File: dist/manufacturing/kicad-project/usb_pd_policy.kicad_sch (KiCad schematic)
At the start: 20 parts, among them Q2 CSD17484F4, Q3 CSD17484F4, U2 TPS26750SRSMR, U3 M24512-RMN6TP

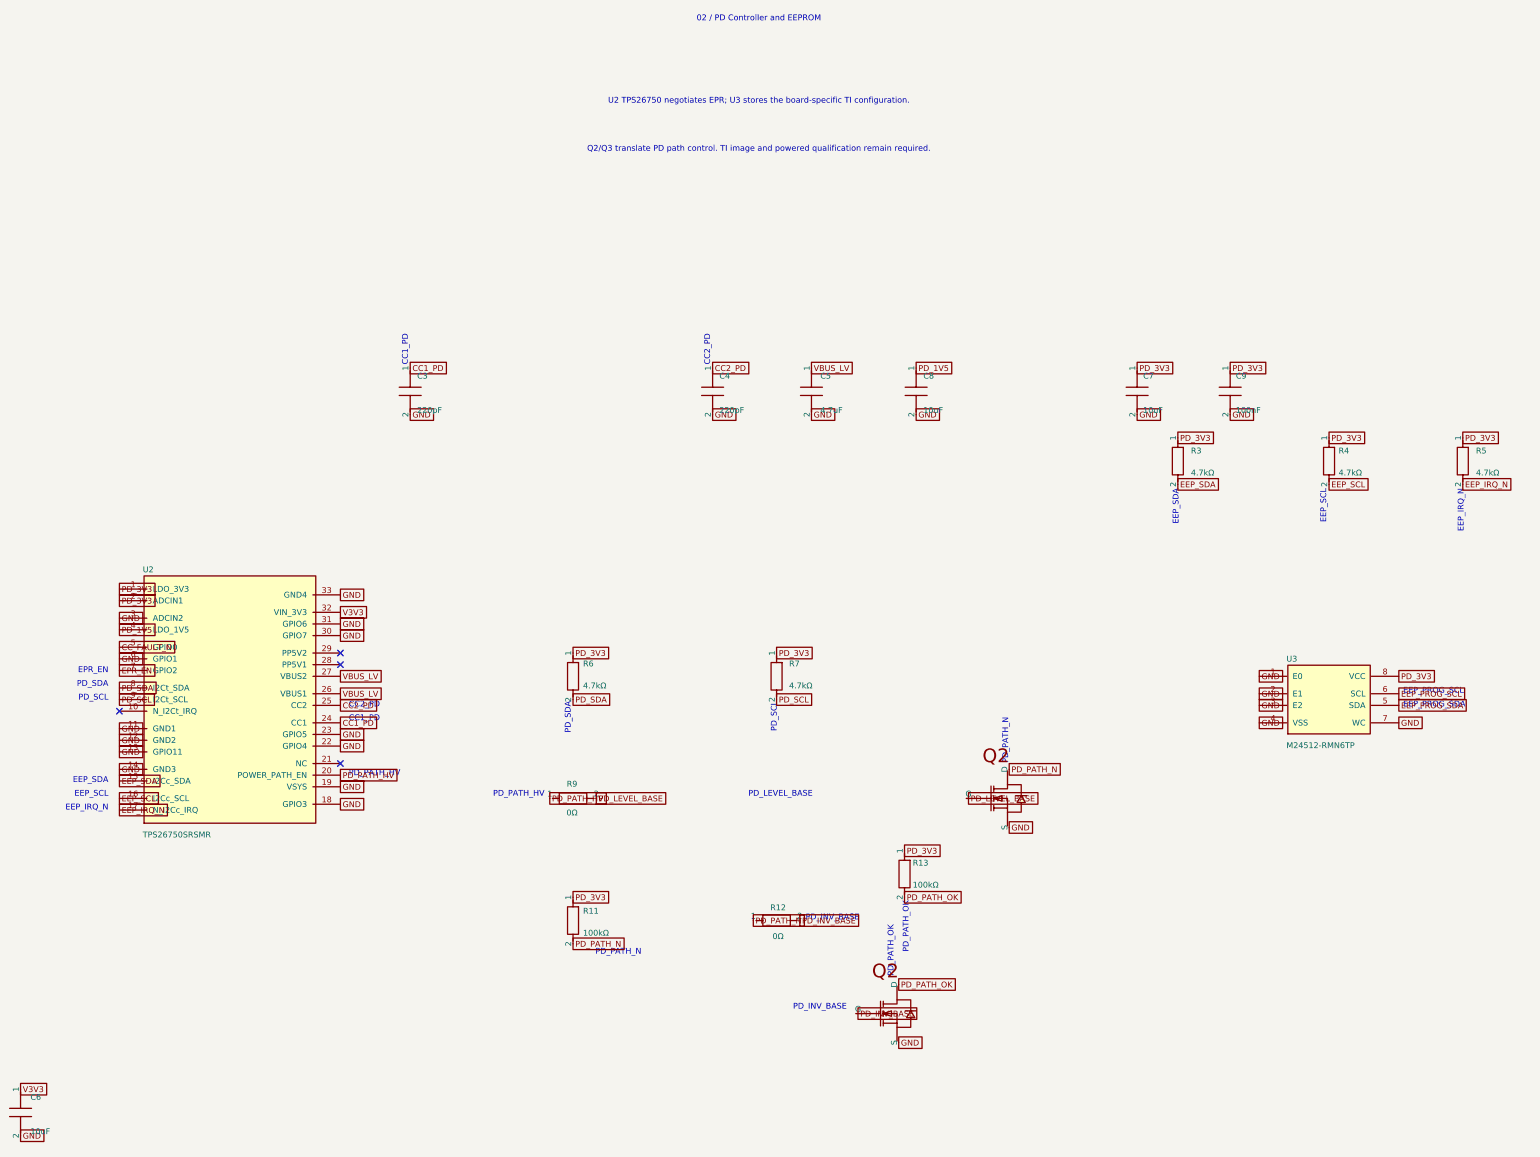
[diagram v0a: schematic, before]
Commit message: Implement motor harness and mounting; remove unsupported interfaces
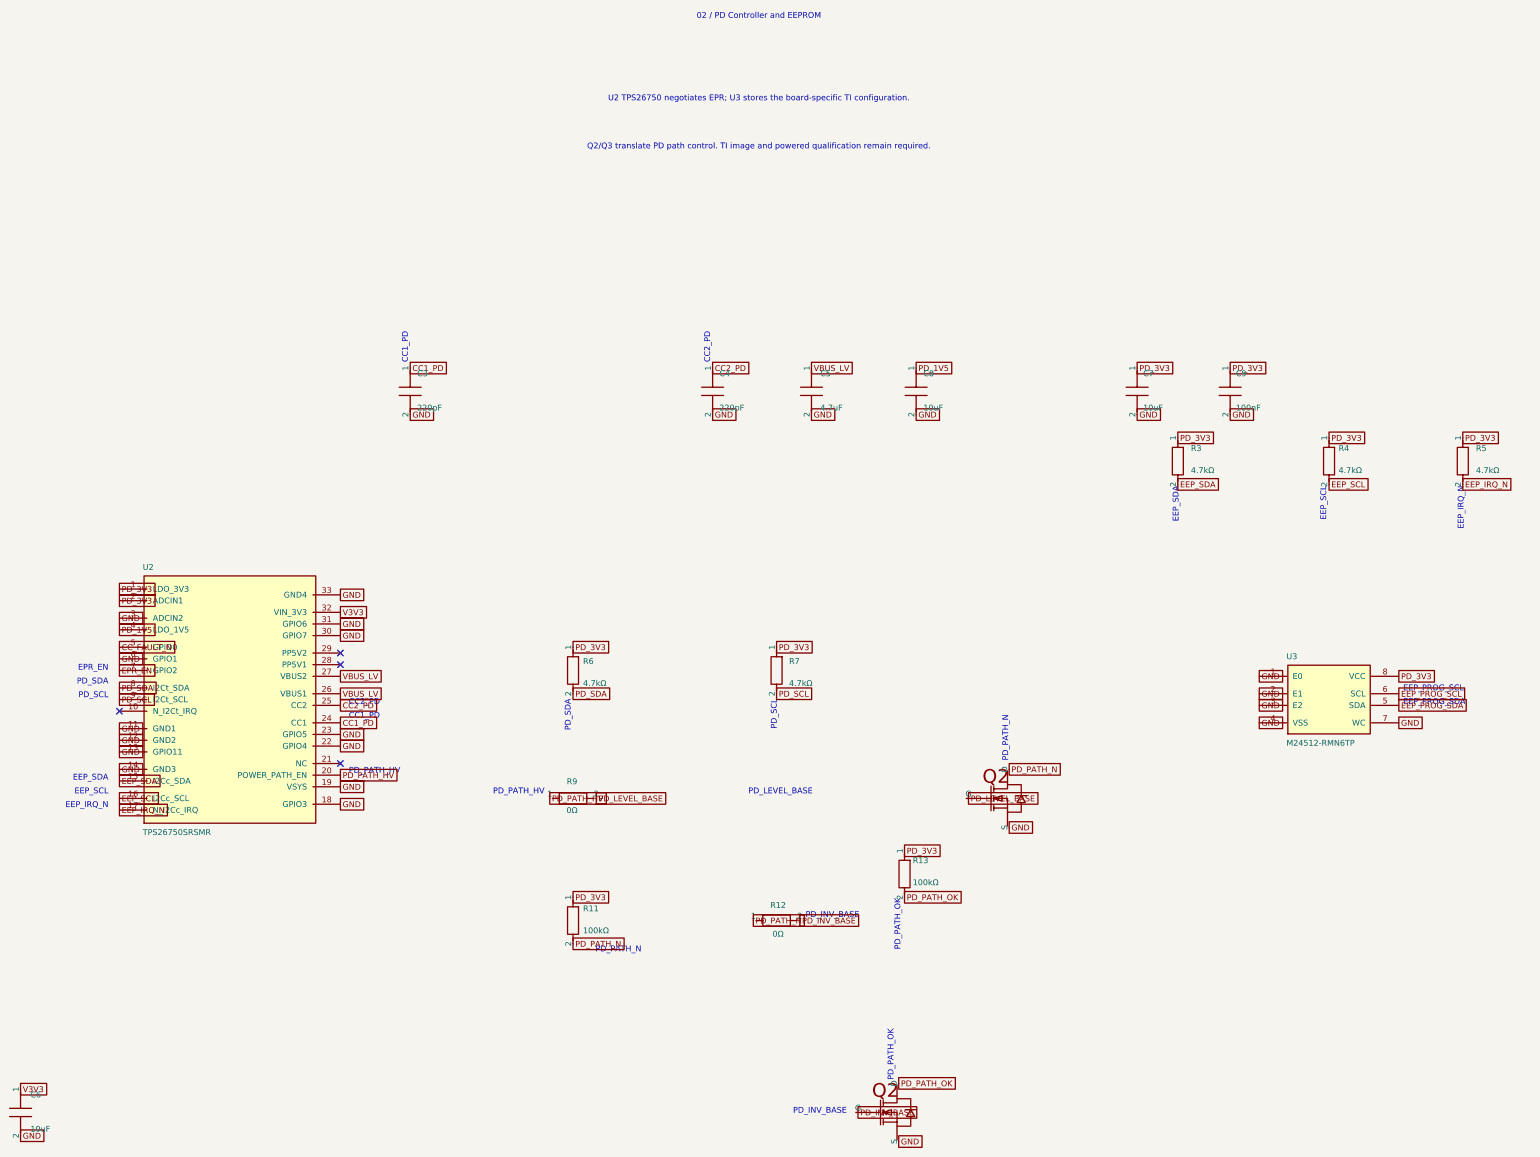
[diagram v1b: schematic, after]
